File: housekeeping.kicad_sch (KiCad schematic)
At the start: 0 parts

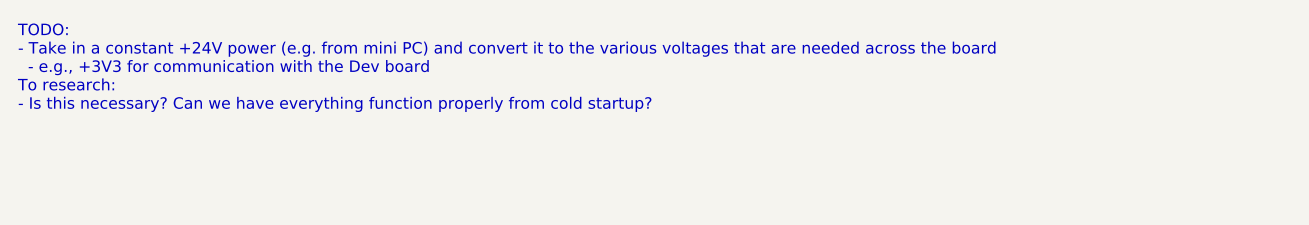
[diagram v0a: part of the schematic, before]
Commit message: Added in & out data from each subsheet
For more details, please contact @leftisttachyon on Discord
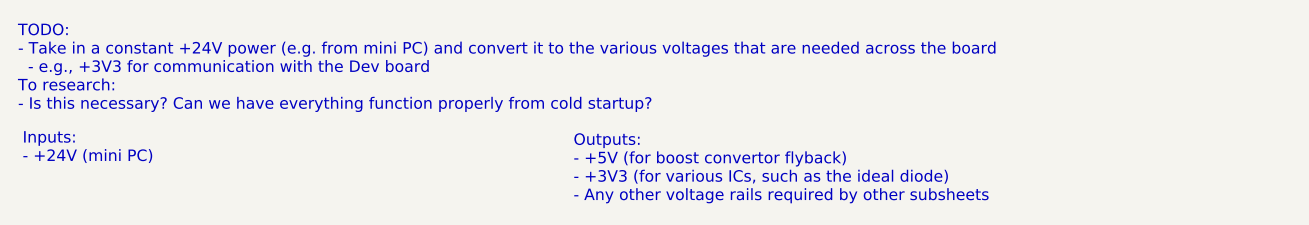
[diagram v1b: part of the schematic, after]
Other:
- note added: "Inputs: - +24V (mini PC)"
- note added: "Outputs: - +5V (for boost convertor flyback) - +3V3 (for various ICs, such as the ideal diode) - Any other voltage rails required by other subsheets"
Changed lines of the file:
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@@
 	(generator_version "8.0")
 	(paper "A4")
+	(text "Outputs:\n- +5V (for boost convertor flyback)\n- +3V3 (for various ICs, such as the ideal diode)\n- Any other voltage rails required by other subsheets"
+		(exclude_from_sim no)
+		(at 148.336 108.712 0)
+		(effects
+			(font
+				(size 1.27 1.27)
+			)
+			(justify left top)
+		)
+	)
+	(text "Inputs:\n- +24V (mini PC)"
+		(exclude_from_sim no)
+		(at 87.122 108.458 0)
+		(effects
+			(font
+				(size 1.27 1.27)
+			)
+			(justify left top)
+		)
+	)
 	(text "TODO:\n- Take in a constant +24V power (e.g. from mini PC) and convert it to the various voltages that are needed across the board\n  - e.g., +3V3 for communication with the Dev board\nTo research:\n- Is this necessary? Can we have everything function properly from cold startup?"
 		(exclude_from_sim no)

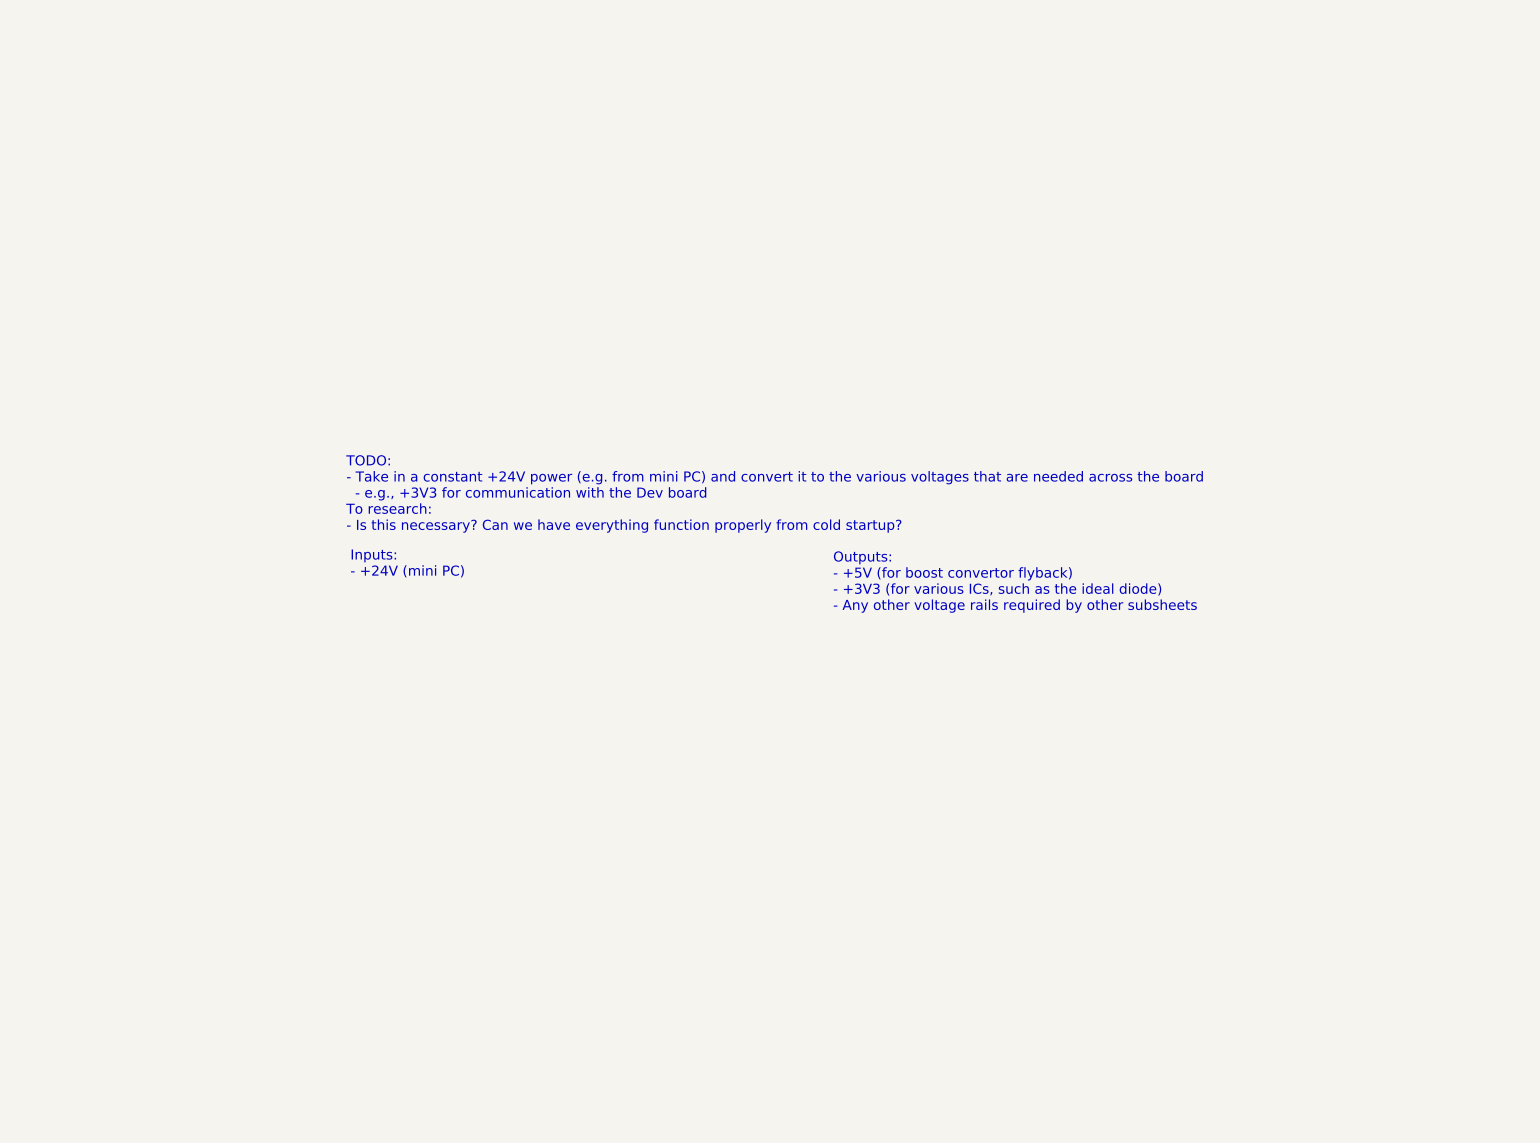
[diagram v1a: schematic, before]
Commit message: Completed first version of housekeeping supplies
+5V and +3V3 from mini PC +24V
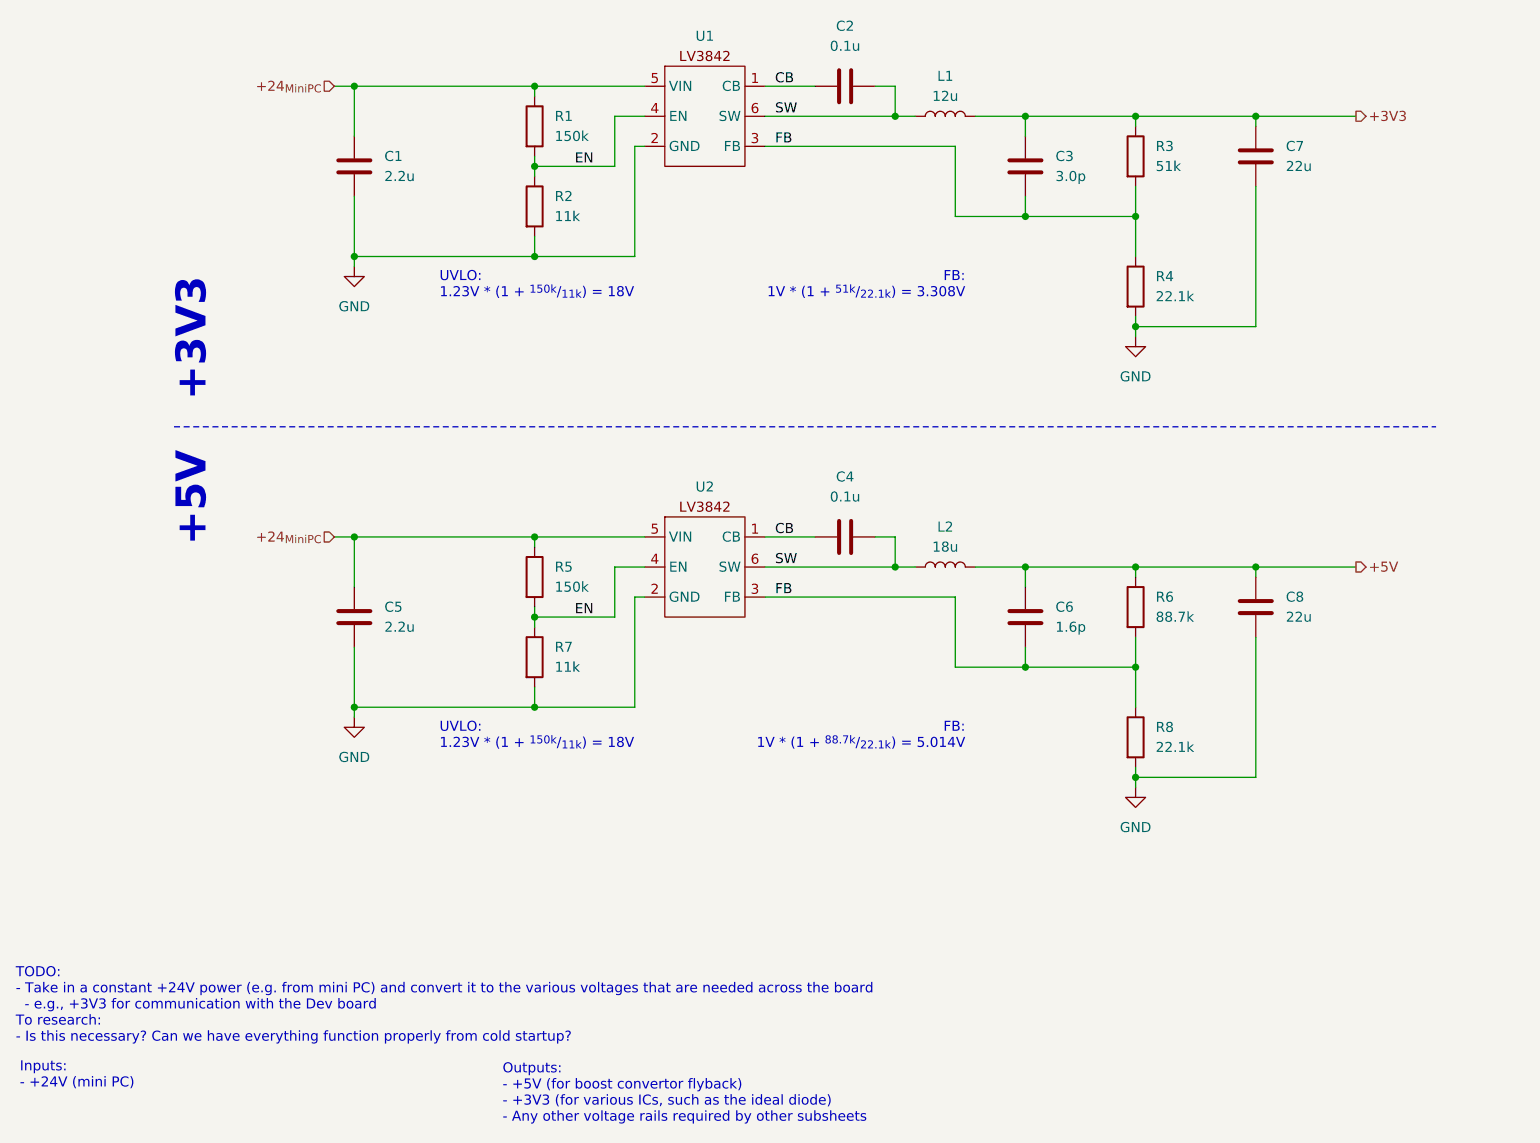
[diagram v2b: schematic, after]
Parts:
- added C1, C5: 2.2u, Capacitor_SMD:C_0603_1608Metric_Pad1.08x0.95mm_HandSolder, symbol Device:C
- added C2, C4: 0.1u, Capacitor_SMD:C_0603_1608Metric_Pad1.08x0.95mm_HandSolder, symbol Device:C
- added C3: 3.0p, Capacitor_SMD:C_0603_1608Metric_Pad1.08x0.95mm_HandSolder, symbol Device:C
- added C6: 1.6p, Capacitor_SMD:C_0603_1608Metric_Pad1.08x0.95mm_HandSolder, symbol Device:C
- added C7, C8: 22u, Capacitor_SMD:C_0603_1608Metric_Pad1.08x0.95mm_HandSolder, symbol Device:C
- added L1: 12u, symbol Device:L
- added L2: 18u, symbol Device:L
- added R1, R5: 150k, Resistor_SMD:R_0603_1608Metric_Pad0.98x0.95mm_HandSolder, symbol Device:R
- added R2, R7: 11k, Resistor_SMD:R_0603_1608Metric_Pad0.98x0.95mm_HandSolder, symbol Device:R
- added R3: 51k, Resistor_SMD:R_0603_1608Metric_Pad0.98x0.95mm_HandSolder, symbol Device:R
- added R4, R8: 22.1k, Resistor_SMD:R_0603_1608Metric_Pad0.98x0.95mm_HandSolder, symbol Device:R
- added R6: 88.7k, Resistor_SMD:R_0603_1608Metric_Pad0.98x0.95mm_HandSolder, symbol Device:R
- added U1, U2: ~, Package_TO_SOT_SMD:SOT-23-6_Handsoldering, symbol ! Robomaster:LV3842
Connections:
- new net +24_{MiniPC}: C1.1, C5.1, R1.1, R5.1, U1.5 (VIN), U2.5 (VIN)
- new net +3V3: C3.2, C7.1, L1.2, R3.1
- new net +5V: C6.2, C8.1, L2.2, R6.1
- new net CB: C2.1, C4.1, U1.1 (CB), U2.1 (CB)
- new net EN: R1.2, R2.1, R5.2, R7.1, U1.4 (EN), U2.4 (EN)
- new net FB: C3.1, C6.1, R3.2, R4.1, R6.2, R8.1, U1.3 (FB), U2.3 (FB)
- new net GND: C1.2, C5.2, C7.2, C8.2, R2.2, R4.2, R7.2, R8.2, U1.2 (GND), U2.2 (GND)
- new net SW: C2.2, C4.2, L1.1, L2.1, U1.6 (SW), U2.6 (SW)
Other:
- note added: "+3V3"
- note added: "+5V"
- note added: "FB: 1V * (1 + ^{51k}/_{22.1k}) = 3.308V"
- note added: "FB: 1V * (1 + ^{88.7k}/_{22.1k}) = 5.014V"
- note added: "UVLO: 1.23V * (1 + ^{150k}/_{11k}) = 18V"
- company: (none) -> UT Robomaster
- title: (none) -> Housekeeping Power Supplies

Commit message: Adjust documentation
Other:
- note added: "UVLO (on): 1.23V * (1 + ^{150k}/_{11k}) = 18V"
- note removed: "UVLO: 1.23V * (1 + ^{150k}/_{11k}) = 18V"
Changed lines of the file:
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@@
 	(text "FB:\n1V * (1 + ^{51k}/_{22.1k}) = 3.308V"
 		(exclude_from_sim no)
-		(at 165.1 73.025 0)
+		(at 180.34 73.025 0)
 		(effects
 			(font
@@
 		)
 	)
-	(text "UVLO:\n1.23V * (1 + ^{150k}/_{11k}) = 18V\n"
+	(text "UVLO (on):\n1.23V * (1 + ^{150k}/_{11k}) = 18V\n"
 		(exclude_from_sim no)
 		(at 98.425 130.175 0)
@@
 		)
 	)
-	(text "UVLO:\n1.23V * (1 + ^{150k}/_{11k}) = 18V\n"
+	(text "UVLO (on):\n1.23V * (1 + ^{150k}/_{11k}) = 18V\n"
 		(exclude_from_sim no)
 		(at 98.425 73.025 0)
@@
 	(text "FB:\n1V * (1 + ^{88.7k}/_{22.1k}) = 5.014V"
 		(exclude_from_sim no)
-		(at 165.1 130.175 0)
+		(at 179.07 130.175 0)
 		(effects
 			(font
